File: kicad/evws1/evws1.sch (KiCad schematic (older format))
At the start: 66 parts, among them J1 Screw_Terminal_01x03, J10 Screw_Terminal_01x04, J2 Screw_Terminal_01x02, J3 HB9500-2P, J4 HB9500-3P, J5 Screw_Terminal_01x04, J6 Screw_Terminal_01x03, J7 Screw_Terminal_01x02, J8 HB9500-2P, J9 HB9500-3P, K1 G3MB-202P, K2 G3MB-202P, M1 HLK-PM01, M2 dc-dc-buck-converter-5v-to-3.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, M3 dc-dc-converter-5v-to-p12v-m1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, Q1 AO3401, Q2 AO3401, SW1 SW_SS13F06-G5, SW2 SW_SS13F06-G5, T1 ZMPT101B, T2 ZMPT101B, U2 ACS712-30, U3 ACS712-30

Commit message: ...
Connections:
- wire segments 254 -> 257
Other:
- moved on the sheet: C2, C4, D13, D3, J2, J3, J4, J5, J6, K1, Q1, R10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

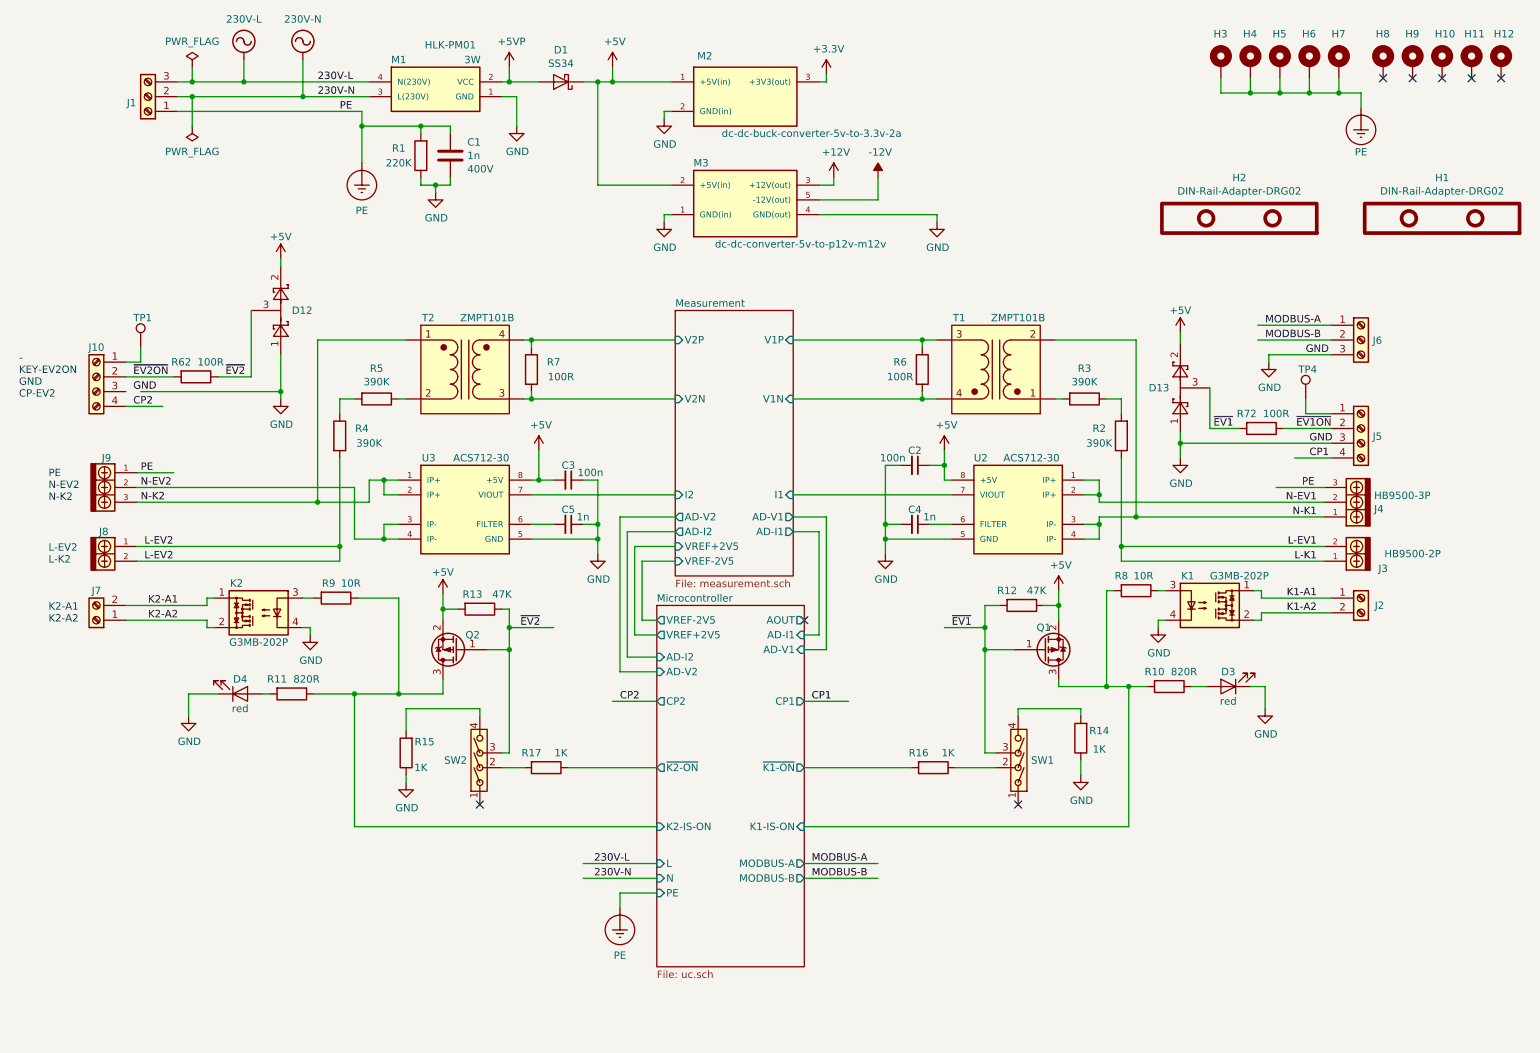
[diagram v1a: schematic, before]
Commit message: Schematic completed, no DRC errors left
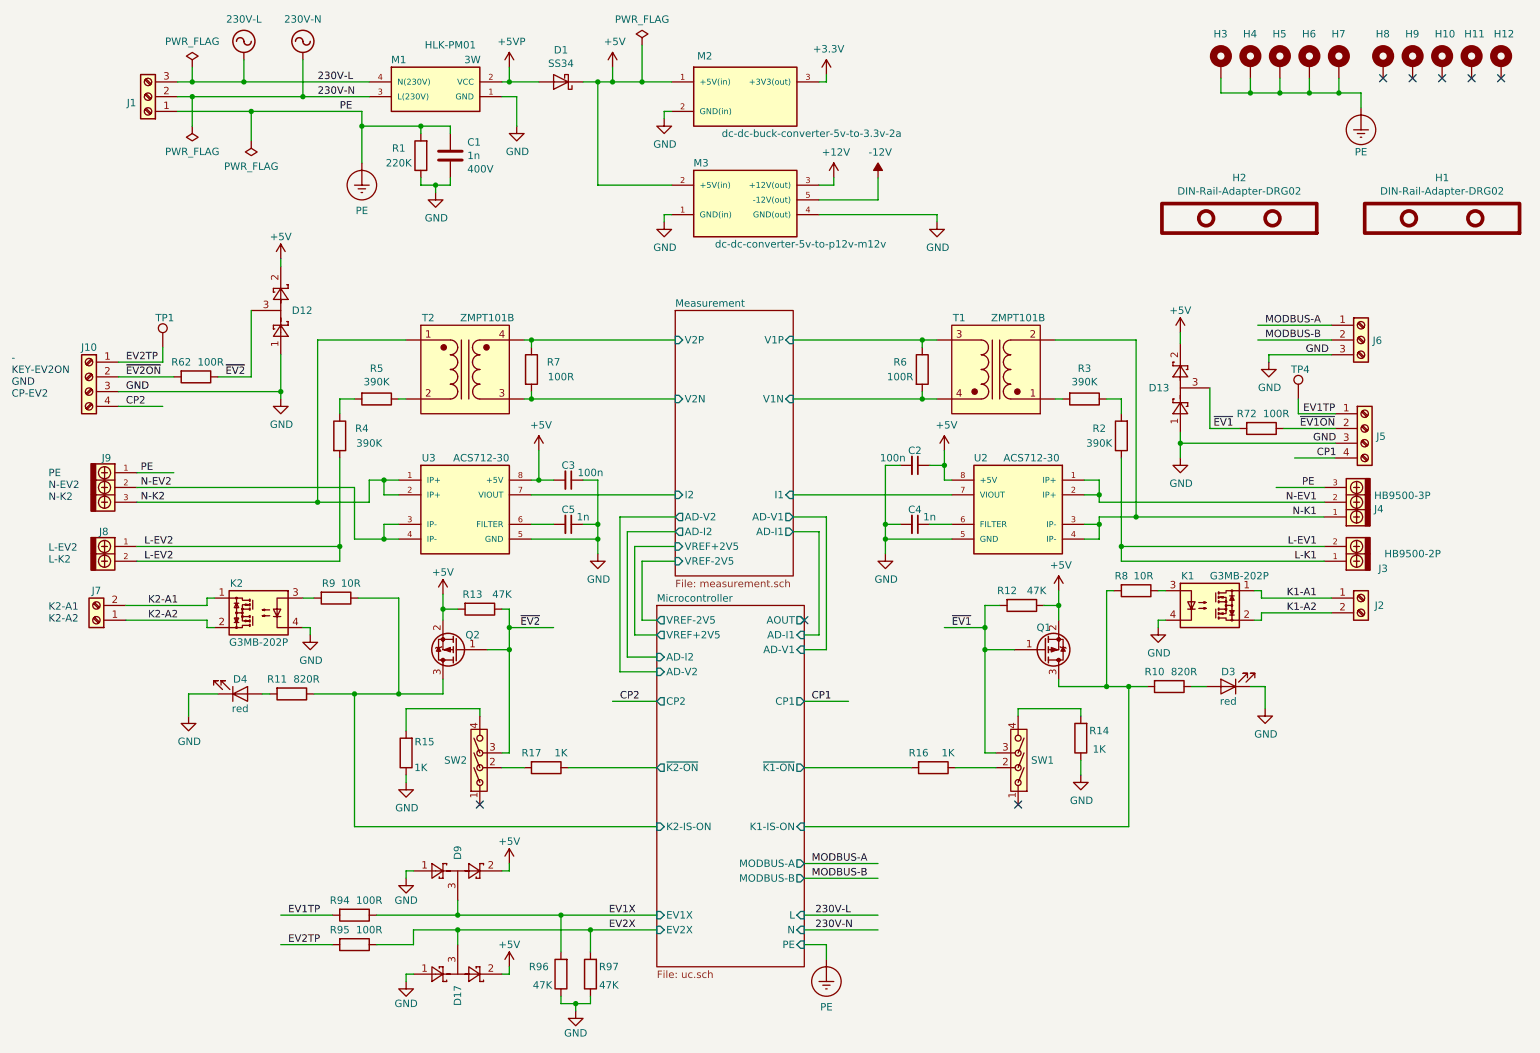
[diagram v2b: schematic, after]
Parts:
- added D17, D9: BAT54S, Project:sot-23_hand-soldering, symbol _project:BAT54S
- added R94, R95: 100R, Project:r-0805-hand-soldering, symbol Device:R
- added R96, R97: 47K, Project:r-0805-hand-soldering, symbol Device:R
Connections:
- net labels added: EV1TP, EV1X, EV2TP, EV2X
- wire segments 257 -> 288
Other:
- moved on the sheet: J10, J5, TP1, TP4

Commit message: schematic finished
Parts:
- removed R6, R7: 100R, Project:r-0805-hand-soldering, symbol Device:R
- R1: value 220K -> 0R; footprint Project:r-0805-hand-soldering -> Project:r-1206-hand-soldering
- R62, R72: value 100R -> 180R
- R94, R95: value 100R -> 330R
- TP1, TP4: footprint Measurement_Points:Measurement_Point_Round-TH_Big -> Measurement_Points:Measurement_Point_Round-TH_Small
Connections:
- net labels removed: L-K1
- wire segments 288 -> 284
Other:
- note added: "K1-A1\nK1-A2"
- note added: "L-EV1\nL-K1"
- note added: "PE\nN-EV1\nN-K1"
- moved on the sheet: D1, J2, J3, K1, R2, R3, R8, TP1, TP4

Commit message: ...
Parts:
- R10, R11, R12, R13, R14, R15, R16, R17, R2, R3, R4, R5, R62, R72, R8, R9, R94, R95, R96, R97: footprint Project:r-0805-hand-soldering -> Project:r-1206-hand-soldering
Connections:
- no-connect marks 8 -> 7
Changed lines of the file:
@@
 F 0 "R2" H 8500 2950 50  0000 C CNN
 F 1 "390K" H 8500 3050 50  0000 C CNN
-F 2 "Project:r-0805-hand-soldering" V 8280 3000 50  0001 C CNN
+F 2 "Project:r-1206-hand-soldering" V 8280 3000 50  0001 C CNN
 F 3 "~" H 8350 3000 50  0001 C CNN
 	1    8350 3000
@@
 F 0 "R5" V 3043 3200 50  0000 C CNN
 F 1 "390K" V 3134 3200 50  0000 C CNN
-F 2 "Project:r-0805-hand-soldering" V 3180 3200 50  0001 C CNN
+F 2 "Project:r-1206-hand-soldering" V 3180 3200 50  0001 C CNN
 F 3 "~" H 3250 3200 50  0001 C CNN
 	1    3250 3200
@@
 F 0 "R4" H 3150 3500 50  0000 C CNN
 F 1 "390K" H 3200 3400 50  0000 C CNN
-F 2 "Project:r-0805-hand-soldering" V 2930 3450 50  0001 C CNN
+F 2 "Project:r-1206-hand-soldering" V 2930 3450 50  0001 C CNN
 F 3 "~" H 3000 3450 50  0001 C CNN
 	1    3000 3450
@@
 F 0 "R3" V 7893 2800 50  0000 C CNN
 F 1 "390K" V 7984 2800 50  0000 C CNN
-F 2 "Project:r-0805-hand-soldering" V 8030 2800 50  0001 C CNN
+F 2 "Project:r-1206-hand-soldering" V 8030 2800 50  0001 C CNN
 F 3 "~" H 8100 2800 50  0001 C CNN
 	1    8100 2800
@@
 F 0 "R9" V 2875 4500 50  0000 C CNN
 F 1 "10R" V 2875 4650 50  0000 C CNN
-F 2 "Project:r-0805-hand-soldering" V 2905 4550 50  0001 C CNN
+F 2 "Project:r-1206-hand-soldering" V 2905 4550 50  0001 C CNN
 F 3 "~" H 2975 4550 50  0001 C CNN
 	1    2975 4550
@@
 F 0 "R8" V 8300 4450 50  0000 C CNN
 F 1 "10R" V 8300 4600 50  0000 C CNN
-F 2 "Project:r-0805-hand-soldering" V 8330 4550 50  0001 C CNN
+F 2 "Project:r-1206-hand-soldering" V 8330 4550 50  0001 C CNN
 F 3 "~" H 8400 4550 50  0001 C CNN
 	1    8400 4550
@@
 F 0 "R11" V 2575 5100 50  0000 C CNN
 F 1 "820R" V 2575 5300 50  0000 C CNN
-F 2 "Project:r-0805-hand-soldering" V 2605 5200 50  0001 C CNN
+F 2 "Project:r-1206-hand-soldering" V 2605 5200 50  0001 C CNN
 F 3 "~" H 2675 5200 50  0001 C CNN
 	1    2675 5200
@@
 F 0 "R13" V 3850 4575 50  0000 C CNN
 F 1 "47K" V 3850 4775 50  0000 C CNN
-F 2 "Project:r-0805-hand-soldering" V 3880 4625 50  0001 C CNN
+F 2 "Project:r-1206-hand-soldering" V 3880 4625 50  0001 C CNN
 F 3 "~" H 3950 4625 50  0001 C CNN
 	1    3950 4625
@@
 F 0 "R15" H 3325 5525 50  0000 C CNN
 F 1 "1K" H 3350 5700 50  0000 C CNN
-F 2 "Project:r-0805-hand-soldering" V 3380 5600 50  0001 C CNN
+F 2 "Project:r-1206-hand-soldering" V 3380 5600 50  0001 C CNN
 F 3 "~" H 3450 5600 50  0001 C CNN
 	1    3450 5600
@@
 F 0 "R10" V 8725 5075 50  0000 C CNN
 F 1 "820R" V 8725 5275 50  0000 C CNN
-F 2 "Project:r-0805-hand-soldering" V 8555 5150 50  0001 C CNN
+F 2 "Project:r-1206-hand-soldering" V 8555 5150 50  0001 C CNN
 F 3 "~" H 8625 5150 50  0001 C CNN
 	1    8625 5150
@@
 F 0 "R12" V 7525 4500 50  0000 C CNN
 F 1 "47K" V 7525 4700 50  0000 C CNN
-F 2 "Project:r-0805-hand-soldering" V 7555 4600 50  0001 C CNN
+F 2 "Project:r-1206-hand-soldering" V 7555 4600 50  0001 C CNN
 F 3 "~" H 7625 4600 50  0001 C CNN
 	1    7625 4600
@@
 F 0 "R17" V 4300 5600 50  0000 C CNN
 F 1 "1K" V 4300 5800 50  0000 C CNN
-F 2 "Project:r-0805-hand-soldering" V 4330 5700 50  0001 C CNN
+F 2 "Project:r-1206-hand-soldering" V 4330 5700 50  0001 C CNN
 F 3 "~" H 4400 5700 50  0001 C CNN
 	1    4400 5700
@@
 F 0 "R16" V 6925 5600 50  0000 C CNN
 F 1 "1K" V 6925 5800 50  0000 C CNN
-F 2 "Project:r-0805-hand-soldering" V 6955 5700 50  0001 C CNN
+F 2 "Project:r-1206-hand-soldering" V 6955 5700 50  0001 C CNN
 F 3 "~" H 7025 5700 50  0001 C CNN
 	1    7025 5700
@@
 $EndComp
 Wire Wire Line
-	6075 4100 6250 4100
-Wire Wire Line
-	6250 4100 6250 4800
-Wire Wire Line
-	6250 4800 6150 4800
-Wire Wire Line
-	6075 4000 6300 4000
-Wire Wire Line
-	6300 4000 6300 4900
-Wire Wire Line
-	6300 4900 6150 4900
+	6075 4100 6400 4100
+Wire Wire Line
+	6400 4100 6400 4800
+Wire Wire Line
+	6400 4800 6150 4800
+Wire Wire Line
+	6075 4000 6450 4000
+Wire Wire Line
+	6450 4000 6450 4900
+Wire Wire Line
+	6450 4900 6150 4900
 Wire Wire Line
 	5275 4100 4950 4100
@@
 U 1 1 5E039DE1
 P 9925 2800
-F 0 "J6" H 9900 3000 50  0000 L CNN
+F 0 "J6" H 9900 2600 50  0000 L CNN
 F 1 "Screw_Terminal_01x03" H 10005 2751 50  0001 L CNN
 F 2 "Project:Terminalblock-5mm-3P" H 9925 2800 50  0001 C CNN
 F 3 "~" H 9925 2800 50  0001 C CNN
 	1    9925 2800
-	1    0    0    -1
+	1    0    0    1
 $EndComp
 Wire Wire Line
@@
 L Connector:Screw_Terminal_01x04 J5
 U 1 1 5E12902A
-P 9950 3400
-F 0 "J5" H 9925 3600 50  0000 L CNN
-F 1 "Screw_Terminal_01x04" H 9870 3626 50  0001 C CNN
-F 2 "Project:Terminalblock-5mm-4P" H 9950 3400 50  0001 C CNN
-F 3 "~" H 9950 3400 50  0001 C CNN
-	1    9950 3400
-	1    0    0    -1
+P 9950 3500
+F 0 "J5" H 9925 3200 50  0000 L CNN
+F 1 "Screw_Terminal_01x04" H 9870 3726 50  0001 C CNN
+F 2 "Project:Terminalblock-5mm-4P" H 9950 3500 50  0001 C CNN
+F 3 "~" H 9950 3500 50  0001 C CNN
+	1    9950 3500
+	1    0    0    1
 $EndComp
 Wire Wire Line
@@
 F6 "AD-I2" I L 5150 4950 50
 F7 "AD-V2" I L 5150 5050 50
-F8 "AOUT" O R 6150 4700 50
-F9 "PE" I R 6150 6900 50
-F10 "MODBUS-A" O R 6150 6350 50
-F11 "MODBUS-B" O R 6150 6450 50
-F12 "K1-IS-ON" I R 6150 6100 50
-F13 "~K1-ON" O R 6150 5700 50
-F14 "L" I R 6150 6700 50
-F15 "N" I R 6150 6800 50
-F16 "K2-IS-ON" I L 5150 6100 50
-F17 "~K2-ON" O L 5150 5700 50
-F18 "VREF+2V5" O L 5150 4800 50
-F19 "VREF-2V5" O L 5150 4700 50
-F20 "EV1X" I L 5150 6700 50
-F21 "EV2X" I L 5150 6800 50
+F8 "PE" I R 6150 6900 50
+F9 "MODBUS-A" O R 6150 6350 50
+F10 "MODBUS-B" O R 6150 6450 50
+F11 "K1-IS-ON" I R 6150 6100 50
+F12 "~K1-ON" O R 6150 5700 50
+F13 "L" I R 6150 6700 50
+F14 "N" I R 6150 6800 50
+F15 "K2-IS-ON" I L 5150 6100 50
+F16 "~K2-ON" O L 5150 5700 50
+F17 "VREF+2V5" O L 5150 4800 50
+F18 "VREF-2V5" O L 5150 4700 50
+F19 "EV1X" I L 5150 6700 50
+F20 "EV2X" I L 5150 6800 50
 $EndSheet
 Wire Wire Line
@@
 F 0 "R14" H 7900 5450 50  0000 C CNN
 F 1 "1K" H 7900 5575 50  0000 C CNN
-F 2 "Project:r-0805-hand-soldering" V 7955 5500 50  0001 C CNN
+F 2 "Project:r-1206-hand-soldering" V 7955 5500 50  0001 C CNN
 F 3 "~" H 8025 5500 50  0001 C CNN
 	1    8025 5500
@@
 F 0 "R72" V 9150 3300 50  0000 C CNN
 F 1 "180R" V 9150 3500 50  0000 C CNN
-F 2 "Project:r-0805-hand-soldering" V 9180 3400 50  0001 C CNN
+F 2 "Project:r-1206-hand-soldering" V 9180 3400 50  0001 C CNN
 F 3 "~" H 9250 3400 50  0001 C CNN
 	1    9250 3400
@@
 F 0 "R62" V 1925 2950 50  0000 C CNN
 F 1 "180R" V 1925 3150 50  0000 C CNN
-F 2 "Project:r-0805-hand-soldering" V 1955 3050 50  0001 C CNN
+F 2 "Project:r-1206-hand-soldering" V 1955 3050 50  0001 C CNN
 F 3 "~" H 2025 3050 50  0001 C CNN
 	1    2025 3050
@@
 Wire Wire Line
 	5000 4200 5275 4200
-NoConn ~ 6150 4700
 Wire Wire Line
 	9725 4600 9250 4600
@@
 F 0 "R96" H 4650 7050 50  0000 C CNN
 F 1 "47K" H 4625 7175 50  0000 C CNN
-F 2 "Project:r-0805-hand-soldering" V 4430 7100 50  0001 C CNN
+F 2 "Project:r-1206-hand-soldering" V 4430 7100 50  0001 C CNN
 F 3 "~" H 4500 7100 50  0001 C CNN
 	1    4500 7100
@@
 F 0 "R97" H 4575 7050 50  0000 C CNN
 F 1 "47K" H 4575 7175 50  0000 C CNN
-F 2 "Project:r-0805-hand-soldering" V 4630 7100 50  0001 C CNN
+F 2 "Project:r-1206-hand-soldering" V 4630 7100 50  0001 C CNN
 F 3 "~" H 4700 7100 50  0001 C CNN
 	1    4700 7100
@@
 F 0 "R94" V 3000 6600 50  0000 C CNN
 F 1 "330R" V 3000 6800 50  0000 C CNN
-F 2 "Project:r-0805-hand-soldering" V 3030 6700 50  0001 C CNN
+F 2 "Project:r-1206-hand-soldering" V 3030 6700 50  0001 C CNN
 F 3 "~" H 3100 6700 50  0001 C CNN
 	1    3100 6700
@@
 AR Path="/5E0A3961/5F6ED0C4/5E90F923" Ref="D?"  Part="1"
 AR Path="/5E90F923" Ref="D9"  Part="1"
-F 0 "D9" V 3800 6475 50  0000 L CNN
+F 0 "D9" H 3750 6500 50  0000 L CNN
 F 1 "BAT54S" V 3755 6488 50  0001 L CNN
 F 2 "Project:sot-23_hand-soldering" H 3875 6525 50  0001 L CNN
@@
 AR Path="/5E0A3961/5F6ED0C4/5E9388FC" Ref="D?"  Part="1"
 AR Path="/5E9388FC" Ref="D17"  Part="1"
-F 0 "D17" V 3800 7175 50  0000 L CNN
+F 0 "D17" H 3750 7225 50  0000 L CNN
 F 1 "BAT54S" V 3755 7188 50  0001 L CNN
 F 2 "Project:sot-23_hand-soldering" H 3875 7225 50  0001 L CNN
@@
 F 0 "R95" V 3200 6800 50  0000 C CNN
 F 1 "330R" V 3200 7025 50  0000 C CNN
-F 2 "Project:r-0805-hand-soldering" V 3030 6900 50  0001 C CNN
+F 2 "Project:r-1206-hand-soldering" V 3030 6900 50  0001 C CNN
 F 3 "~" H 3100 6900 50  0001 C CNN
 	1    3100 6900

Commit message: ...
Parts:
- M1: footprint Project:HLK-PM01 -> Project:HLK-PM01-5M05
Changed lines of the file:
@@
 F 0 "M1" H 3400 1400 50  0000 C CNN
 F 1 "HLK-PM01" H 3750 1400 50  0000 C CNN
-F 2 "Project:HLK-PM01" H 3650 1050 50  0001 C CIN
+F 2 "Project:HLK-PM01-5M05" H 3650 1050 50  0001 C CIN
 F 3 "" H 3650 850 50  0001 C CNN
 F 4 "3W" H 3900 1000 50  0000 C CNN "P"

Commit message: ...
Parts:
- added J21, J22: header, Project:idc-header-1x04-p2.54mm-vertical, symbol Connector_Generic:Conn_01x04
- renumbered R4 to R90, R5 to R93, TP4 to TP2
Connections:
- net labels added: AD-I1, AD-I2, AD-V1, AD-V2
- wire segments 284 -> 295
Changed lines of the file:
@@
 $EndComp
 $Comp
-L Device:R R5
+L Device:R R93
 U 1 1 5E1A9D87
 P 3250 3200
-F 0 "R5" V 3043 3200 50  0000 C CNN
+F 0 "R93" V 3043 3200 50  0000 C CNN
 F 1 "390K" V 3134 3200 50  0000 C CNN
 F 2 "Project:r-1206-hand-soldering" V 3180 3200 50  0001 C CNN
@@
 $EndComp
 $Comp
-L Device:R R4
+L Device:R R90
 U 1 1 5E1A9E53
 P 3000 3450
-F 0 "R4" H 3150 3500 50  0000 C CNN
+F 0 "R90" H 3150 3500 50  0000 C CNN
 F 1 "390K" H 3200 3400 50  0000 C CNN
 F 2 "Project:r-1206-hand-soldering" V 2930 3450 50  0001 C CNN
@@
 	6150 6450 6650 6450
 Wire Wire Line
-	4850 5250 5150 5250
+	4625 5250 5150 5250
 Text Label 6200 6350 0    50   ~ 0
 MODBUS-A
 Text Label 6200 6450 0    50   ~ 0
 MODBUS-B
-Text Label 4900 5250 0    50   ~ 0
+Text Label 4625 5250 0    50   ~ 0
 CP2
 Wire Wire Line
@@
 CP1
 Wire Wire Line
-	6150 5250 6450 5250
-Text Label 6200 5250 0    50   ~ 0
+	6150 5250 6750 5250
+Text Label 6750 5250 2    50   ~ 0
 CP1
 $Comp
@@
 $EndComp
 Wire Wire Line
-	6075 4100 6400 4100
-Wire Wire Line
-	6400 4100 6400 4800
-Wire Wire Line
-	6400 4800 6150 4800
+	6075 4100 6300 4100
+Wire Wire Line
+	6300 4100 6300 4800
+Wire Wire Line
+	6300 4800 6150 4800
 Wire Wire Line
 	6075 4000 6450 4000
@@
 ~EV1ON
 $Comp
-L Connector:TestPoint TP4
+L Connector:TestPoint TP2
 U 1 1 5EC3C43D
 P 9500 3250
-F 0 "TP4" H 9450 3450 50  0000 L CNN
+F 0 "TP2" H 9450 3450 50  0000 L CNN
 F 1 "TestPoint" H 9558 3279 50  0001 L CNN
 F 2 "Measurement_Points:Measurement_Point_Round-TH_Small" H 9700 3250 50  0001 C CNN
@@
 Wire Wire Line
 	7050 3200 6075 3200
+$Comp
+L Connector_Generic:Conn_01x04 J21
+U 1 1 5E422024
+P 6950 5250
+F 0 "J21" H 6950 4950 50  0000 C CNN
+F 1 "header" H 6925 5450 50  0000 C CNN
+F 2 "Project:idc-header-1x04-p2.54mm-vertical" H 6950 5250 50  0001 C CNN
+F 3 "~" H 6950 5250 50  0001 C CNN
+	1    6950 5250
+	1    0    0    1
+$EndComp
+$Comp
+L power:GND #PWR0258
+U 1 1 5E43948B
+P 6675 5400
+F 0 "#PWR0258" H 6675 5150 50  0001 C CNN
+F 1 "GND" H 6680 5227 50  0000 C CNN
+F 2 "" H 6675 5400 50  0001 C CNN
+F 3 "" H 6675 5400 50  0001 C CNN
+	1    6675 5400
+	1    0    0    -1
+$EndComp
+Wire Wire Line
+	6750 5350 6675 5350
+Wire Wire Line
+	6675 5350 6675 5400
+Connection ~ 6300 4800
+$Comp
+L Connector_Generic:Conn_01x04 J22
+U 1 1 5E4E08A3
+P 4425 5250
+F 0 "J22" H 4425 4950 50  0000 C CNN
+F 1 "header" H 4400 5450 50  0000 C CNN
+F 2 "Project:idc-header-1x04-p2.54mm-vertical" H 4425 5250 50  0001 C CNN
+F 3 "~" H 4425 5250 50  0001 C CNN
+	1    4425 5250
+	-1   0    0    1
+$EndComp
+$Comp
+L power:GND #PWR0259
+U 1 1 5E50FCB6
+P 4700 5400
+F 0 "#PWR0259" H 4700 5150 50  0001 C CNN
+F 1 "GND" H 4705 5227 50  0000 C CNN
+F 2 "" H 4700 5400 50  0001 C CNN
+F 3 "" H 4700 5400 50  0001 C CNN
+	1    4700 5400
+	1    0    0    -1
+$EndComp
+Wire Wire Line
+	4625 5350 4700 5350
+Wire Wire Line
+	4700 5350 4700 5400
+Wire Wire Line
+	4625 5050 4900 5050
+Connection ~ 4900 5050
+Wire Wire Line
+	4950 4950 4950 5150
+Wire Wire Line
+	4625 5150 4950 5150
+Connection ~ 4950 4950
+Wire Wire Line
+	6300 5150 6750 5150
+Wire Wire Line
+	6300 4800 6300 5150
+Wire Wire Line
+	6750 5050 6450 5050
+Wire Wire Line
+	6450 5050 6450 4900
+Connection ~ 6450 4900
+Text Label 4625 5150 0    50   ~ 0
+AD-I2
+Text Label 4625 5050 0    50   ~ 0
+AD-V2
+Text Label 6750 5150 2    50   ~ 0
+AD-I1
+Text Label 6750 5050 2    50   ~ 0
+AD-V1
 $EndSCHEMATC
